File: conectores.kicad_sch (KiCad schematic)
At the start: 20 parts, among them J1 12v Input, J12 Temp, J2 Fan1, J3 Fan2, J4 Fan4, J5 Fan3, J7 OLED, U3 LM2575

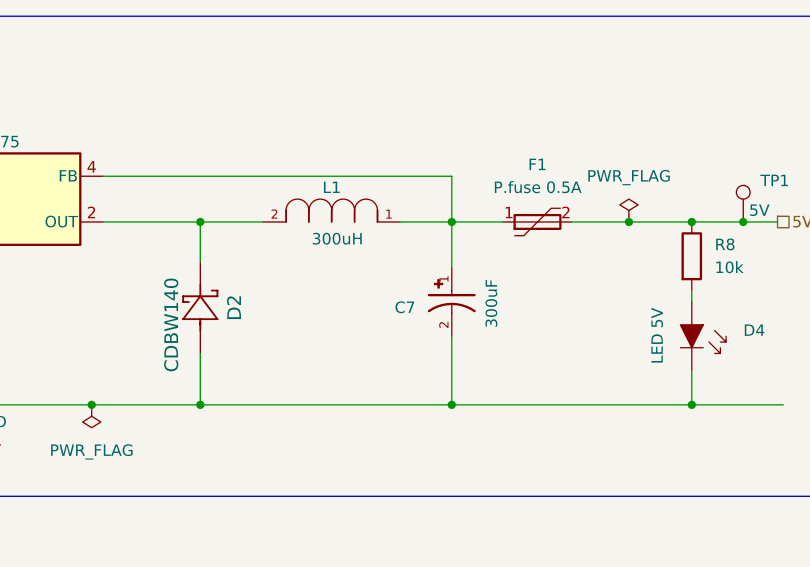
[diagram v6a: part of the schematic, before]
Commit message: minor changes
- Change L/C values 300 -> 330
- Change footprint association: 12v pinheader is now vertical
- Change 3D models for capacitors (replaced due to lack of stock)
- Also changed some references to make it more neat
- Add also a square around the fan switch area in the schematic
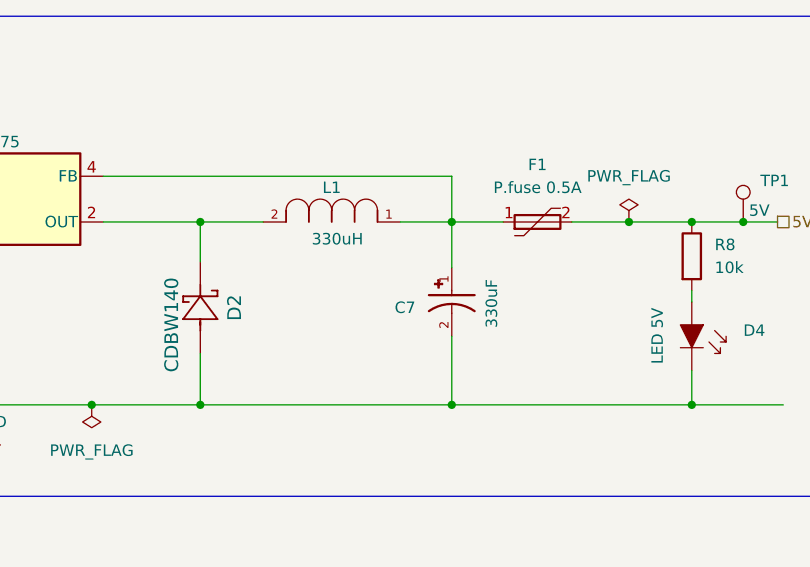
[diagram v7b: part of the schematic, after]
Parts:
- C7: value 300uF -> 330uF
- J1: footprint Connector_PinHeader_2.54mm:PinHeader_1x02_P2.54mm_Horizontal -> Connector_PinHeader_2.54mm:PinHeader_1x02_P2.54mm_Vertical
- L1: value 300uH -> 330uH
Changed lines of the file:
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@@
     (in_bom yes) (on_board yes)
     (property "Reference" "L1" (id 0) (at 176.53 45.085 0))
-    (property "Value" "300uH" (id 1) (at 177.165 50.8 0))
+    (property "Value" "330uH" (id 1) (at 177.165 50.8 0))
     (property "Footprint" "footprints descargados:DR127-331_INDM125125X800N" (id 2) (at 168.91 48.895 0)
       (effects (font (size 1.27 1.27)) (justify bottom) hide)
@@
       (effects (font (size 1.27 1.27)) (justify left))
     )
-    (property "Value" "300uF" (id 1) (at 194.31 55.245 0)
+    (property "Value" "330uF" (id 1) (at 194.31 55.245 0)
       (effects (font (size 1.27 1.27)) (justify left))
     )
@@
       (effects (font (size 1.27 1.27)) (justify right))
     )
-    (property "Footprint" "Connector_PinHeader_2.54mm:PinHeader_1x02_P2.54mm_Horizontal" (id 2) (at 73.025 46.355 0)
-      (effects (font (size 1.27 1.27)) hide)
-    )
+    (property "Footprint" "Connector_PinHeader_2.54mm:PinHeader_1x02_P2.54mm_Vertical" (id 2) (at 73.025 46.355 0)
+      (effects (font (size 1.27 1.27)) hide)
+    )
